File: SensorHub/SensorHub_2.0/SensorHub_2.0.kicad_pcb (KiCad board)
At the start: 2 copper layers, 30 x 28 mm, 60 parts, among them J1 Conn_01x02, J4 USB_C_Receptacle, P1 BM46B-12DP-0.35V_53_, P2 BM46B-12DP-0.35V_53_, U1 R7FA4E2B93CFM#AA0, U2 MYRGM080200C41RA, U3 TJA1051TK-3, U4 BMI270, U5 ASCODV-24.000MHZ-LR-T3

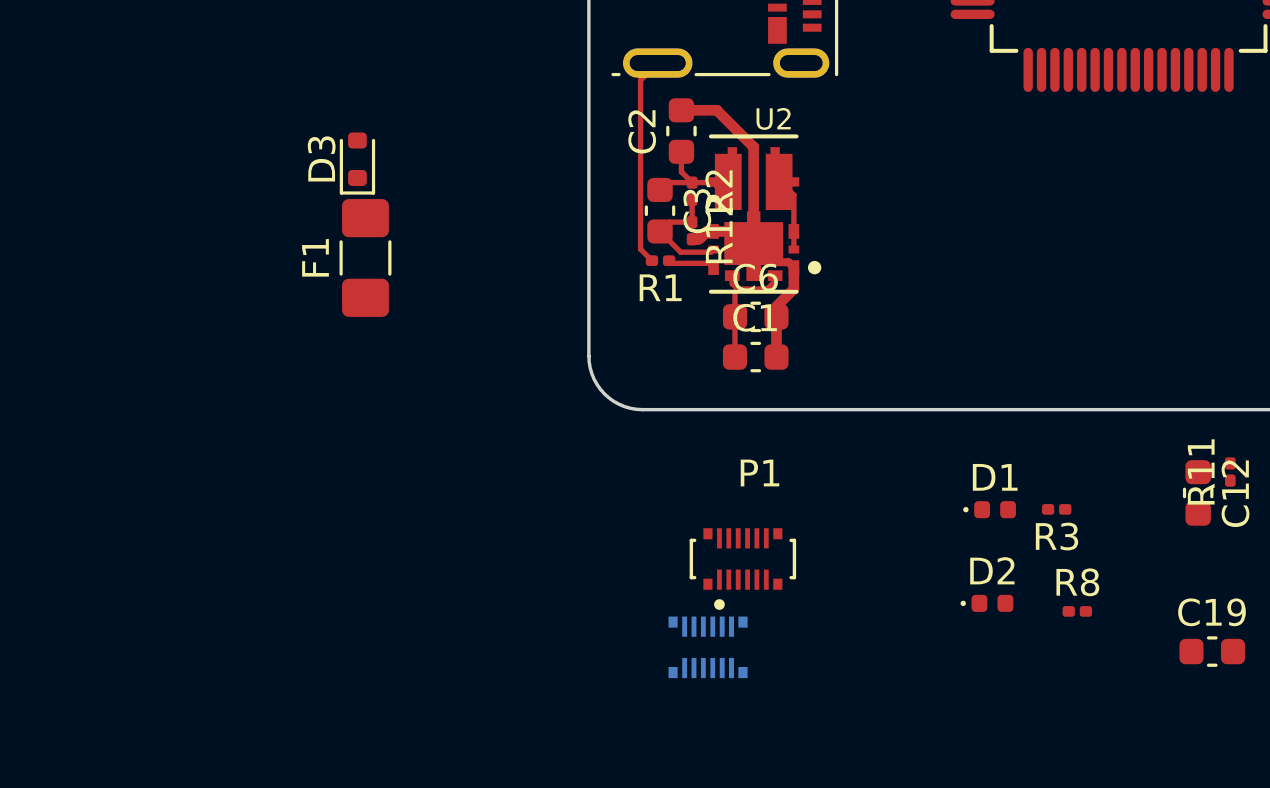
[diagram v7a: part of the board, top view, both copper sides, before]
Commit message: New hierarchy
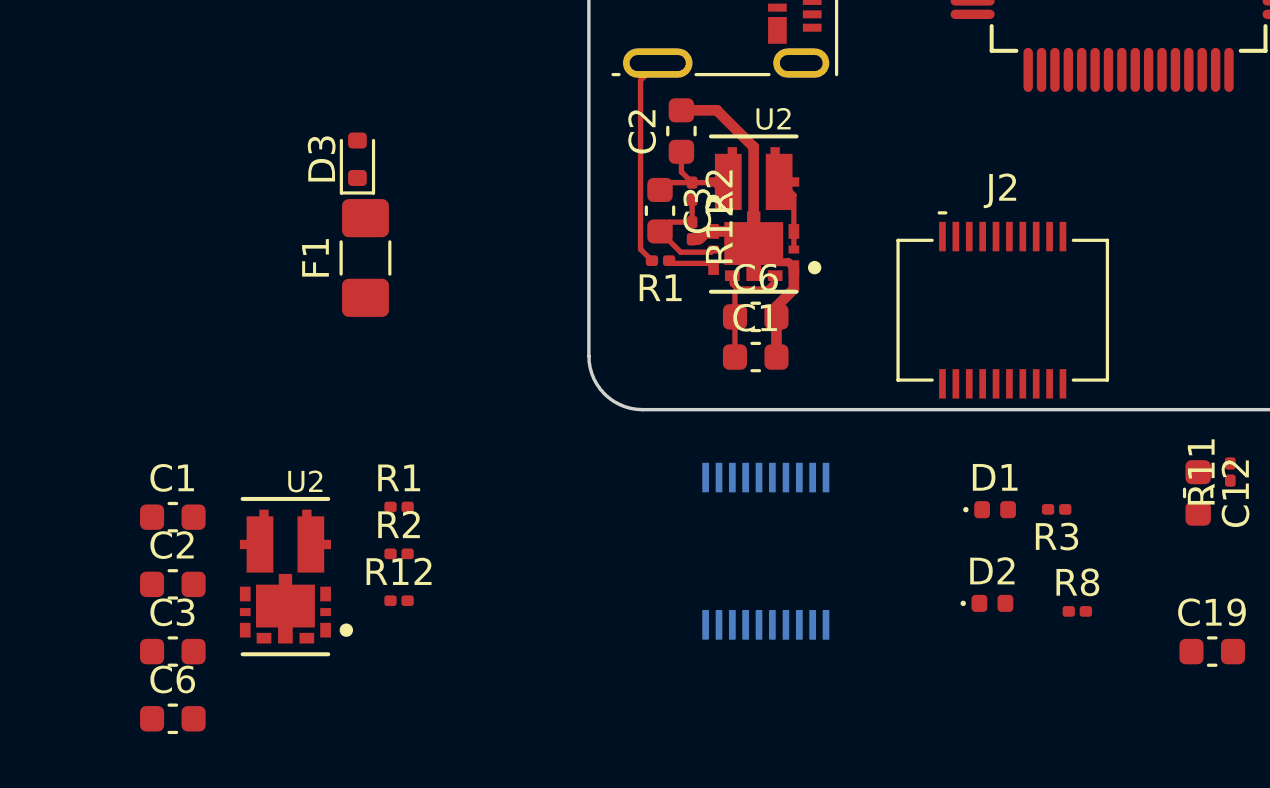
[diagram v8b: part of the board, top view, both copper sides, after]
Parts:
- removed P1, P2: BM46B-12DP-0.35V_53_, BM46B-12DP-0.35V_53_:HRS_BM46B-12DP-0.35V_53_
- added C1: 10V/22uF, Capacitor_SMD:C_0603_1608Metric, F.Cu at (109.4, 129.6)
- added C2: 10V/22uF, Capacitor_SMD:C_0603_1608Metric, F.Cu at (109.4, 132.1)
- added C3: 330 pF, Capacitor_SMD:C_0603_1608Metric, F.Cu at (109.4, 134.6)
- added C6: 16V/1uF, Capacitor_SMD:C_0603_1608Metric, F.Cu at (109.4, 137.1)
- added J2: 658561423020, Connector_SMD_Wurth:J_Wurth_WR-BTB_658561423020, F.Cu at (140.4, 121.8)
- added J3: 658561423020, Connector_SMD_Wurth:J_Wurth_WR-BTB_658561423020, B.Cu at (131.6, 130.8)
- added R1: 10 K, Resistor_SMD:R_0201_0603Metric, F.Cu at (117.9, 129.2)
- added R12: 15 K, Resistor_SMD:R_0201_0603Metric, F.Cu at (117.9, 132.7)
- added R2: 47 K, Resistor_SMD:R_0201_0603Metric, F.Cu at (117.9, 130.9)
- added U2: MYRGM080200C41RA, MYRGM080200C41RA:MURATA_MYRGM080200C41RA_0, F.Cu at (113.6, 131.8)
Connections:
- C4 pad 2: GND -> unconnected-(C4-Pad2)
- U3 pad 2: GND -> Net-(U3-GND-Pad2)
- U3 pad 9: GND -> Net-(U3-GND-Pad2)
